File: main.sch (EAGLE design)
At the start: 46 parts

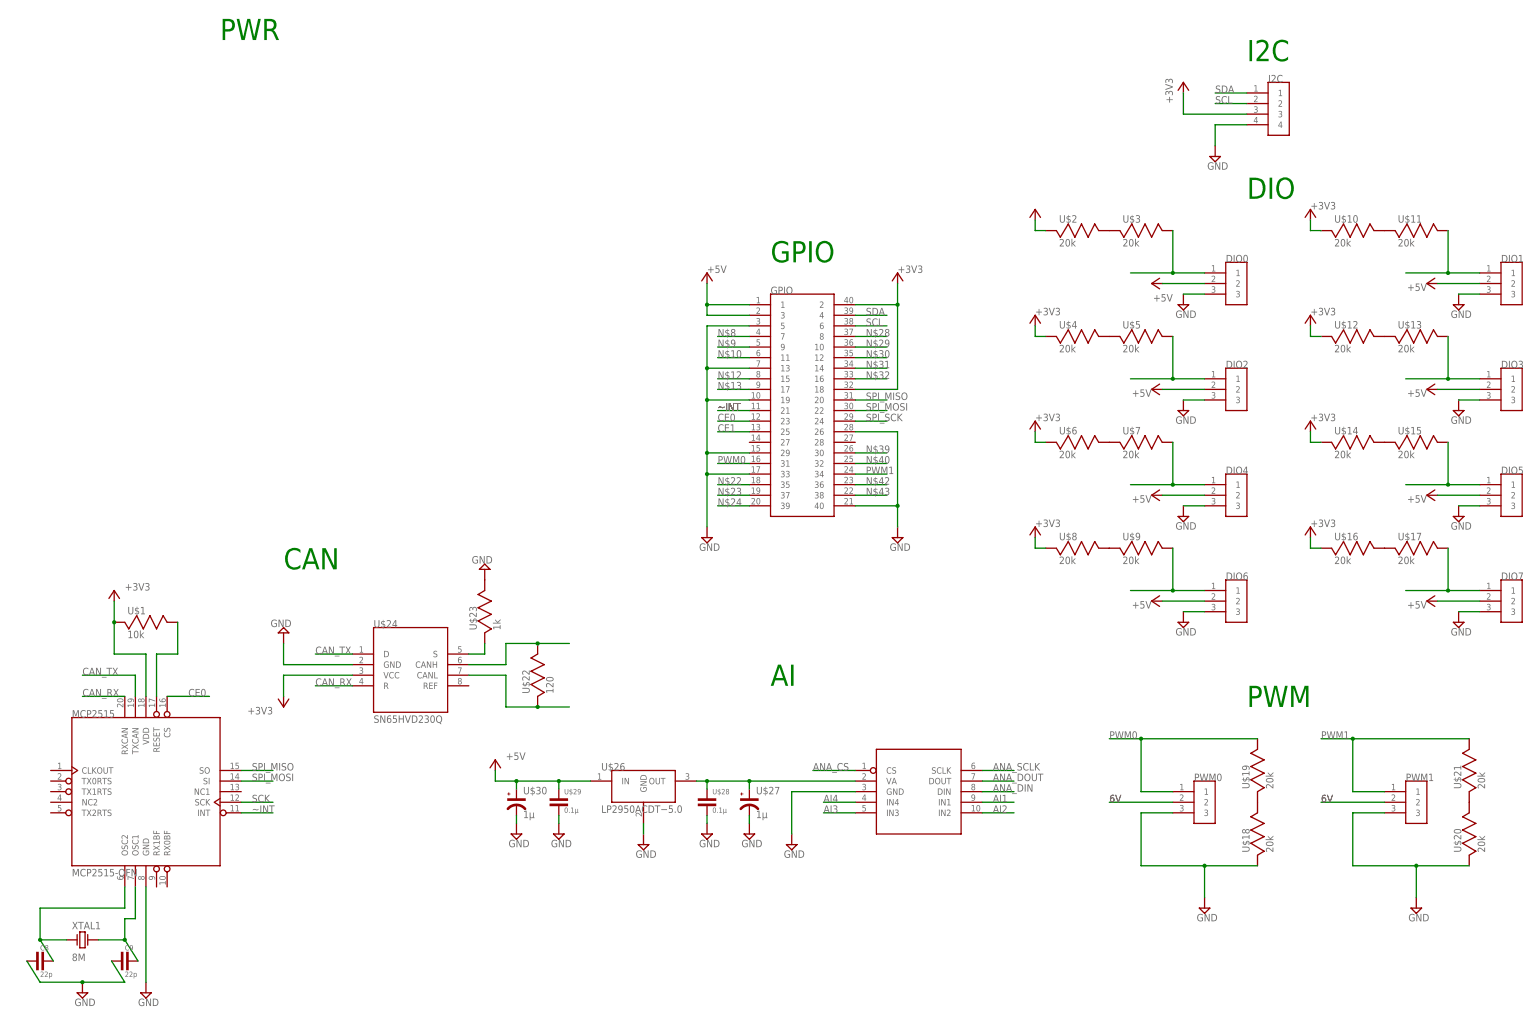
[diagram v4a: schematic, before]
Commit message: power module
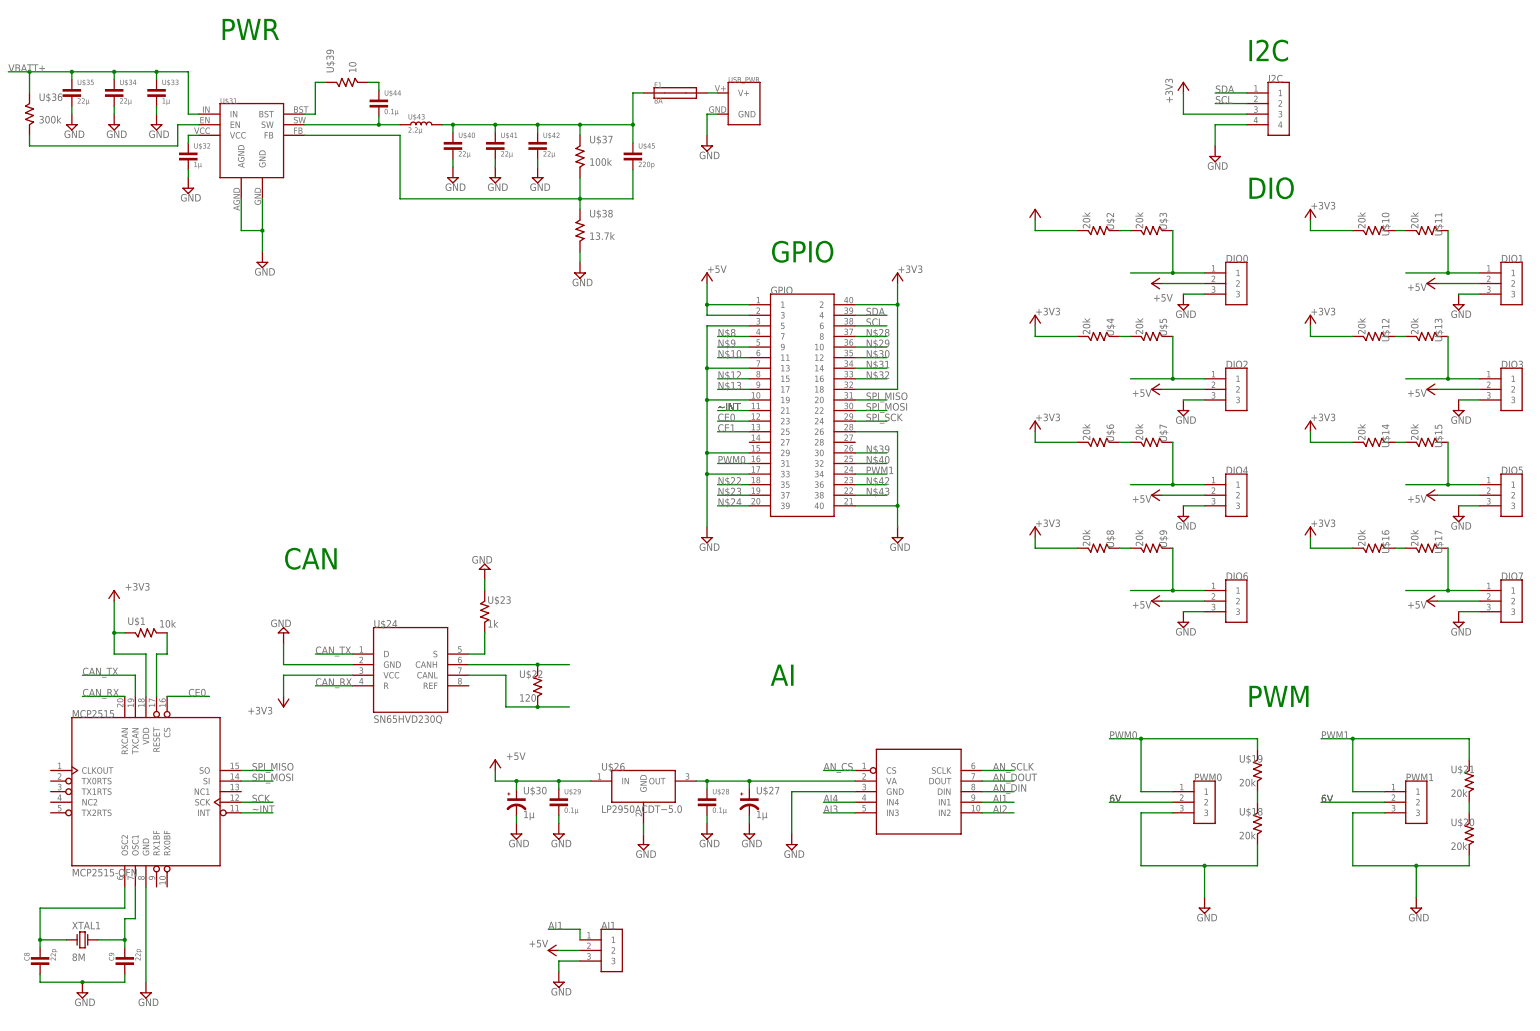
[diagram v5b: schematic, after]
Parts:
- added AI1: 3X1_MALE_HEADER_PIN, SamuelLibrary:3X1_MALE_HEADER_PIN
- added F1: 8A, SamuelLibrary:1206_FUSE
- added U$31: MP2238, SamuelLibrary:MP2238
- added U$32, U$33: 1µ, SamuelLibrary:0603_CAPACITOR
- added U$34, U$35, U$40, U$41, U$42: 22µ, SamuelLibrary:0805_CAPACITOR
- added U$36: 300k, SamuelLibrary:2512_RESISTOR
- added U$37: 100k, SamuelLibrary:2010_RESISTOR
- added U$38: 13.7k, SamuelLibrary:2512_RESISTOR
- added U$39: 10, SamuelLibrary:2512_RESISTOR
- added U$43: 2.2µ, SamuelLibrary:ECS-MPIL0630-2R2MC
- added U$44: 0.1µ, SamuelLibrary:0603_CAPACITOR
- added U$45: 220p, SamuelLibrary:0603_CAPACITOR
- added USB_PWR: USB-C_POWER_PAD, SamuelLibrary:USB-C_POWER_PAD
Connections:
- net ANA_CS renamed AN_CS
- net ANA_DIN renamed AN_DIN
- net ANA_DOUT renamed AN_DOUT
- net ANA_SCLK renamed AN_SCLK
- new net N$1: F1.2, USB_PWR.V+
- new net N$2: U$31.VCC, U$32.L1
- new net N$3: U$31.BST, U$39.P$2
- new net N$4: U$31.EN, U$36.P$1
- new net N$45: U$31.FB, U$37.P$1, U$38.P$2, U$45.L2
- new net N$47: F1.1, U$37.P$2, U$40.L1, U$41.L1, U$42.L1, U$43.P$2, U$45.L1
- new net N$49: U$31.SW, U$43.P$1, U$44.L2
- new net N$50: U$39.P$1, U$44.L1
- new net VBATT+: U$31.IN, U$33.L1, U$34.L1, U$35.L1, U$36.P$2
- net +5V: now also AI1.2
- net AI1: now also AI1.1
- net GND: now also AI1.3, U$31.AGND, U$31.GND, U$32.L2, U$33.L2, U$34.L2, U$35.L2, U$38.P$1, U$40.L2, U$41.L2, U$42.L2, USB_PWR.GND
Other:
- moved on the sheet: C8, C9, U$1, U$10, U$11, U$12, U$13, U$14, U$15, U$16, U$17, U$18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

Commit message: finished schematics parts
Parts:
- added AI2, AI3, AI4: 3X1_MALE_HEADER_PIN, SamuelLibrary:3X1_MALE_HEADER_PIN
- added CAN: 1870640000, SamuelLibrary:1870640000
- added COMM: (no value), SamuelLibrary:WL-SBSW_1204_155124RV73200
- added M1: MOSFET, SamuelLibrary:MOSFET
- added PWR: (no value), SamuelLibrary:WL-SMSW_1204_A_155124VS73200A
- added RSL, VIN: 2X1_MALE_HEADER_PIN, SamuelLibrary:2X1_MALE_HEADER_PIN
- added U$46: 10k, SamuelLibrary:1206_RESISTOR
- added U$48, U$49, U$50, U$51, U$52, U$53: 120, SamuelLibrary:0603_RESISTOR
- added U$54, U$55: 10, SamuelLibrary:2512_RESISTOR
- renumbered U$24 to SN65, U$25 to ADC, U$26 to LP2590, U$31 to MP2238
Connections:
- net N$1 renamed V+
- removed net SCK: MCP2515.SCK
- new net N$1: M1.P$3, U$46.P$2, U$49.P$1
- new net N$51: U$49.P$2
- new net N$52: RSL.1, U$48.P$1
- new net N$53: M1.P$1, RSL.2
- new net N$54: COMM.+, U$51.P$2
- new net N$55: U$51.P$1, U$53.P$2
- new net N$56: U$53.P$1, U$55.P$2
- new net N$57: U$52.P$1, U$54.P$2
- new net N$58: U$50.P$1, U$52.P$2
- new net N$59: PWR.+, U$50.P$2
- new net N$60: COMM.R-
- new net N$61: COMM.G/V-
- net +5V: now also AI2.2, AI3.2, AI4.2, U$54.P$1, U$55.P$1
- net AI2: now also AI2.1
- net AI3: now also AI3.1
- net AI4: now also AI4.1
- net GND: now also AI2.3, AI3.3, AI4.3, M1.P$2, PWR.-, U$46.P$1, VIN.2
- net N$34: now also CAN.1
- net N$35: now also CAN.4
- net SPI_SCK: now also MCP2515.SCK
- net VBATT+: now also U$48.P$2, VIN.1
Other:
- note added: "LED"
- note added: "RSL"
- moved on the sheet: GPIO

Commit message: board layout
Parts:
- removed AI4: 3X1_MALE_HEADER_PIN, SamuelLibrary:3X1_MALE_HEADER_PIN
- removed U$22, U$50, U$51, U$52, U$53: 120, SamuelLibrary:0603_RESISTOR
- removed U$23: 1k, SamuelLibrary:1206_RESISTOR
- removed U$36: 300k, SamuelLibrary:2512_RESISTOR
- removed U$42: 22µ, SamuelLibrary:0805_CAPACITOR
- removed U$45: 220p, SamuelLibrary:0603_CAPACITOR
- removed U$54, U$55: 10, SamuelLibrary:2512_RESISTOR
- added AI0: 3X1_MALE_HEADER_PIN, SamuelLibrary:3X1_MALE_HEADER_PIN
- added C10, C11: 22p, SamuelLibrary:0402_CAPACITOR
- added R1: 300k, SamuelLibrary:2512_RESISTOR
- added R31, R32: 165, SamuelLibrary:0805_RESISTOR
- added R6: 120, SamuelLibrary:0603_RESISTOR
- added R7: 1k, SamuelLibrary:1206_RESISTOR
- C8: value 22p -> 22µ; device SamuelLibrary:0402_CAPACITOR -> SamuelLibrary:0805_CAPACITOR
- C9: value 22p -> 220p; device SamuelLibrary:0402_CAPACITOR -> SamuelLibrary:0603_CAPACITOR
- COMM: device SamuelLibrary:WL-SBSW_1204_155124RV73200 -> SamuelLibrary:WL-SBCC_0603_150060RV75240
- PWR: device SamuelLibrary:WL-SMSW_1204_A_155124VS73200A -> SamuelLibrary:WL-SMCC_0603_R_V_Y_150060VS73220
- renumbered ADC to ADC124S051, U$1 to R5, U$10 to R10, U$11 to R11, U$12 to R14, U$13 to R15, U$14 to R18, U$15 to R19, U$16 to R22, U$17 to R23, U$18 to R25, U$19 to R24, U$2 to R8, U$20 to R27, U$21 to R26, U$27 to C15, U$28 to C14, U$29 to C13, U$3 to R9, U$30 to C12, U$32 to C4, U$33 to C3, U$34 to C2, U$35 to C1, U$37 to R3, U$38 to R4, U$39 to R2, U$4 to R12, U$40 to C6, U$41 to C7, U$43 to L1, U$44 to C5, U$46 to R30, U$48 to R28, U$49 to R29, U$5 to R13, U$6 to R16, U$7 to R17, U$8 to R20, U$9 to R21
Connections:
- net N$18 renamed DIO4
- net N$19 renamed DIO6
- net N$26 renamed DIO7
- net N$37 renamed DIO5
- net N$44 renamed DIO3
- net N$46 renamed DIO1
- net N$5 renamed DIO0
- net N$51 renamed RSL
- net N$7 renamed DIO2
- removed net AI4: ADC124S051.IN4, AI4.1
- removed net N$23: GPIO.37
- removed net N$24: GPIO.39
- removed net N$43: GPIO.38
- removed net N$55: U$51.P$1, U$53.P$2
- removed net N$57: U$52.P$1, U$54.P$2
- removed net N$58: U$50.P$1, U$52.P$2
- removed net N$59: PWR.+, U$50.P$2
- removed net N$60: COMM.R-
- removed net N$61: COMM.G/V-
- new net AI0: ADC124S051.IN1, AI0.1
- new net COMM_GRN: COMM.V+, GPIO.37
- new net COMM_RED: COMM.R+, GPIO.38
- new net PWR: GPIO.39, R31.P$1
- net +5V: now also AI0.2; no longer AI4.2, U$54.P$1, U$55.P$1
- net AI1: now also ADC124S051.IN2; no longer ADC124S051.IN1
- net AI2: now also ADC124S051.IN3; no longer ADC124S051.IN2
- net AI3: now also ADC124S051.IN4; no longer ADC124S051.IN3
- net GND: now also AI0.3, C10.L1, C11.L1, C8.L2, R32.P$1, R7.P$2; no longer AI4.3, C8.L1, C9.L1, U$23.P$2, U$42.L2
- net N$20: now also C10.L2; no longer C8.L2
- net N$34: now also CAN.2, R6.P$2; no longer U$22.P$2
- net N$35: now also CAN.3, R6.P$1; no longer U$22.P$1
- net N$36: now also R7.P$1; no longer U$23.P$1
- net N$4: now also R1.P$1; no longer U$36.P$1
- net N$41: now also C11.L2; no longer C9.L2
- net N$45: now also C9.L2; no longer U$45.L2
- net N$47: now also C8.L1, C9.L1; no longer U$42.L1, U$45.L1
- net N$54: now also PWR.+, R31.P$2; no longer COMM.+, U$51.P$2
- net N$56: now also COMM.R-, COMM.V-, R32.P$2; no longer U$53.P$1, U$55.P$2
- net VBATT+: now also R1.P$2; no longer U$36.P$2
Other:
- moved on the sheet: AI1, AI2, AI3, C8, C9, CAN, COMM, PWR, SN65

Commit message: power block layout
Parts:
- R2, R4: device SamuelLibrary:2512_RESISTOR -> SamuelLibrary:0603_RESISTOR
- R3: device SamuelLibrary:2010_RESISTOR -> SamuelLibrary:0603_RESISTOR
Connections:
- net GND: now also MP2238.GND@3; no longer MP2238.GND
- net N$49: now also MP2238.SW@1; no longer MP2238.SW
